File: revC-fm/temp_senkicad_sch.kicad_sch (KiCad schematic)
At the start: 4 parts, among them U24 MCP9700AT-E/LT

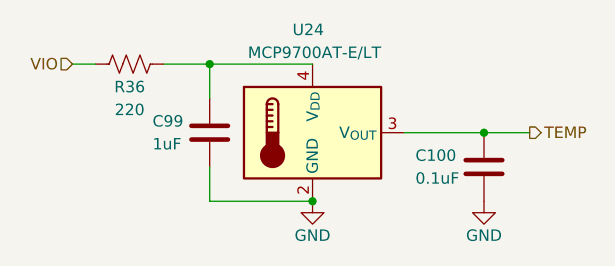
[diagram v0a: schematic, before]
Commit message: updated analog , solar comp, layout
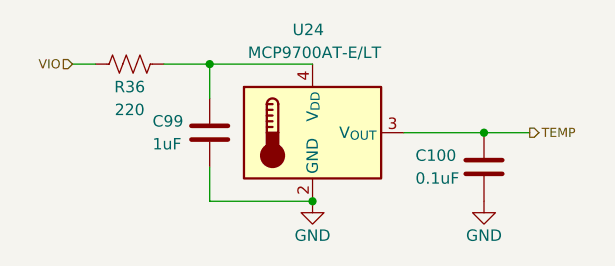
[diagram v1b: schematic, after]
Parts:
- C100: footprint Capacitor_SMD:C_0603_1608Metric -> Capacitor_SMD:C_0402_1005Metric

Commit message: routing
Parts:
- C100: footprint Capacitor_SMD:C_0402_1005Metric -> Capacitor_SMD:C_0603_1608Metric
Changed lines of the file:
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@@
         )
         (path "/d1441985-7b63-4bf8-a06d-c70da2e3b78b/cda1ad7d-3729-4e28-9f04-75ded2a9befd/8821f222-8792-4e4d-9d02-2f4e81ef493f"
-          (reference "#PWR053") (unit 1)
+          (reference "#PWR050") (unit 1)
         )
         (path "/d1441985-7b63-4bf8-a06d-c70da2e3b78b/cda1ad7d-3729-4e28-9f04-75ded2a9befd/795619f3-8bd8-4f29-a923-296e7ed8459e"
-          (reference "#PWR0148") (unit 1)
+          (reference "#PWR0158") (unit 1)
         )
         (path "/d1441985-7b63-4bf8-a06d-c70da2e3b78b/cda1ad7d-3729-4e28-9f04-75ded2a9befd/e299339d-e625-4f2c-804c-bf3cf31a6799"
-          (reference "#PWR0150") (unit 1)
+          (reference "#PWR0160") (unit 1)
         )
         (path "/d1441985-7b63-4bf8-a06d-c70da2e3b78b/cda1ad7d-3729-4e28-9f04-75ded2a9befd/ea7f9fd6-aeb6-4ec9-906e-e84511ddb647"
-          (reference "#PWR0152") (unit 1)
+          (reference "#PWR0162") (unit 1)
         )
       )
@@
         )
         (path "/d1441985-7b63-4bf8-a06d-c70da2e3b78b/cda1ad7d-3729-4e28-9f04-75ded2a9befd/795619f3-8bd8-4f29-a923-296e7ed8459e"
-          (reference "R218") (unit 1)
+          (reference "R211") (unit 1)
         )
         (path "/d1441985-7b63-4bf8-a06d-c70da2e3b78b/cda1ad7d-3729-4e28-9f04-75ded2a9befd/e299339d-e625-4f2c-804c-bf3cf31a6799"
-          (reference "R222") (unit 1)
+          (reference "R215") (unit 1)
         )
         (path "/d1441985-7b63-4bf8-a06d-c70da2e3b78b/cda1ad7d-3729-4e28-9f04-75ded2a9befd/ea7f9fd6-aeb6-4ec9-906e-e84511ddb647"
-          (reference "R223") (unit 1)
+          (reference "R216") (unit 1)
         )
       )
@@
         )
         (path "/d1441985-7b63-4bf8-a06d-c70da2e3b78b/cda1ad7d-3729-4e28-9f04-75ded2a9befd/8821f222-8792-4e4d-9d02-2f4e81ef493f"
-          (reference "U8") (unit 1)
+          (reference "U9") (unit 1)
         )
         (path "/d1441985-7b63-4bf8-a06d-c70da2e3b78b/cda1ad7d-3729-4e28-9f04-75ded2a9befd/795619f3-8bd8-4f29-a923-296e7ed8459e"
-          (reference "U26") (unit 1)
+          (reference "U29") (unit 1)
         )
         (path "/d1441985-7b63-4bf8-a06d-c70da2e3b78b/cda1ad7d-3729-4e28-9f04-75ded2a9befd/e299339d-e625-4f2c-804c-bf3cf31a6799"
-          (reference "U27") (unit 1)
+          (reference "U30") (unit 1)
         )
         (path "/d1441985-7b63-4bf8-a06d-c70da2e3b78b/cda1ad7d-3729-4e28-9f04-75ded2a9befd/ea7f9fd6-aeb6-4ec9-906e-e84511ddb647"
-          (reference "U28") (unit 1)
+          (reference "U31") (unit 1)
         )
       )
@@
         )
         (path "/d1441985-7b63-4bf8-a06d-c70da2e3b78b/cda1ad7d-3729-4e28-9f04-75ded2a9befd/8821f222-8792-4e4d-9d02-2f4e81ef493f"
-          (reference "#PWR052") (unit 1)
+          (reference "#PWR049") (unit 1)
         )
         (path "/d1441985-7b63-4bf8-a06d-c70da2e3b78b/cda1ad7d-3729-4e28-9f04-75ded2a9befd/795619f3-8bd8-4f29-a923-296e7ed8459e"
-          (reference "#PWR0147") (unit 1)
+          (reference "#PWR0157") (unit 1)
         )
         (path "/d1441985-7b63-4bf8-a06d-c70da2e3b78b/cda1ad7d-3729-4e28-9f04-75ded2a9befd/e299339d-e625-4f2c-804c-bf3cf31a6799"
-          (reference "#PWR0149") (unit 1)
+          (reference "#PWR0159") (unit 1)
         )
         (path "/d1441985-7b63-4bf8-a06d-c70da2e3b78b/cda1ad7d-3729-4e28-9f04-75ded2a9befd/ea7f9fd6-aeb6-4ec9-906e-e84511ddb647"
-          (reference "#PWR0151") (unit 1)
+          (reference "#PWR0161") (unit 1)
         )
       )
@@
       (effects (font (size 1.27 1.27)) (justify left))
     )
-    (property "Footprint" "Capacitor_SMD:C_0402_1005Metric" (at 149.5552 104.14 0)
+    (property "Footprint" "Capacitor_SMD:C_0603_1608Metric" (at 149.5552 104.14 0)
       (effects (font (size 1.27 1.27)) hide)
     )
@@
         )
         (path "/d1441985-7b63-4bf8-a06d-c70da2e3b78b/cda1ad7d-3729-4e28-9f04-75ded2a9befd/8821f222-8792-4e4d-9d02-2f4e81ef493f"
-          (reference "C35") (unit 1)
+          (reference "C36") (unit 1)
         )
         (path "/d1441985-7b63-4bf8-a06d-c70da2e3b78b/cda1ad7d-3729-4e28-9f04-75ded2a9befd/795619f3-8bd8-4f29-a923-296e7ed8459e"
-          (reference "C109") (unit 1)
+          (reference "C123") (unit 1)
         )
         (path "/d1441985-7b63-4bf8-a06d-c70da2e3b78b/cda1ad7d-3729-4e28-9f04-75ded2a9befd/e299339d-e625-4f2c-804c-bf3cf31a6799"
-          (reference "C112") (unit 1)
+          (reference "C126") (unit 1)
         )
         (path "/d1441985-7b63-4bf8-a06d-c70da2e3b78b/cda1ad7d-3729-4e28-9f04-75ded2a9befd/ea7f9fd6-aeb6-4ec9-906e-e84511ddb647"
-          (reference "C114") (unit 1)
+          (reference "C128") (unit 1)
         )
       )
@@
         )
         (path "/d1441985-7b63-4bf8-a06d-c70da2e3b78b/cda1ad7d-3729-4e28-9f04-75ded2a9befd/8821f222-8792-4e4d-9d02-2f4e81ef493f"
-          (reference "C34") (unit 1)
+          (reference "C35") (unit 1)
         )
         (path "/d1441985-7b63-4bf8-a06d-c70da2e3b78b/cda1ad7d-3729-4e28-9f04-75ded2a9befd/795619f3-8bd8-4f29-a923-296e7ed8459e"
-          (reference "C108") (unit 1)
+          (reference "C122") (unit 1)
         )
         (path "/d1441985-7b63-4bf8-a06d-c70da2e3b78b/cda1ad7d-3729-4e28-9f04-75ded2a9befd/e299339d-e625-4f2c-804c-bf3cf31a6799"
-          (reference "C111") (unit 1)
+          (reference "C125") (unit 1)
         )
         (path "/d1441985-7b63-4bf8-a06d-c70da2e3b78b/cda1ad7d-3729-4e28-9f04-75ded2a9befd/ea7f9fd6-aeb6-4ec9-906e-e84511ddb647"
-          (reference "C113") (unit 1)
+          (reference "C127") (unit 1)
         )
       )

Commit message: working revC
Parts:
- C100: footprint Capacitor_SMD:C_0603_1608Metric -> Capacitor_SMD:C_0402_1005Metric
- U24: Mfr. Part No (none) -> MCP9700AT-E/LT
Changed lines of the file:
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@@
         )
         (path "/d1441985-7b63-4bf8-a06d-c70da2e3b78b/cda1ad7d-3729-4e28-9f04-75ded2a9befd/8821f222-8792-4e4d-9d02-2f4e81ef493f"
-          (reference "#PWR055") (unit 1)
-        )
-        (path "/d1441985-7b63-4bf8-a06d-c70da2e3b78b/cda1ad7d-3729-4e28-9f04-75ded2a9befd/795619f3-8bd8-4f29-a923-296e7ed8459e"
-          (reference "#PWR0160") (unit 1)
-        )
-        (path "/d1441985-7b63-4bf8-a06d-c70da2e3b78b/cda1ad7d-3729-4e28-9f04-75ded2a9befd/e299339d-e625-4f2c-804c-bf3cf31a6799"
-          (reference "#PWR0162") (unit 1)
-        )
-        (path "/d1441985-7b63-4bf8-a06d-c70da2e3b78b/cda1ad7d-3729-4e28-9f04-75ded2a9befd/ea7f9fd6-aeb6-4ec9-906e-e84511ddb647"
-          (reference "#PWR0164") (unit 1)
+          (reference "#PWR054") (unit 1)
+        )
+        (path "/d1441985-7b63-4bf8-a06d-c70da2e3b78b/cda1ad7d-3729-4e28-9f04-75ded2a9befd/795619f3-8bd8-4f29-a923-296e7ed8459e"
+          (reference "#PWR0140") (unit 1)
+        )
+        (path "/d1441985-7b63-4bf8-a06d-c70da2e3b78b/cda1ad7d-3729-4e28-9f04-75ded2a9befd/e299339d-e625-4f2c-804c-bf3cf31a6799"
+          (reference "#PWR0142") (unit 1)
+        )
+        (path "/d1441985-7b63-4bf8-a06d-c70da2e3b78b/cda1ad7d-3729-4e28-9f04-75ded2a9befd/ea7f9fd6-aeb6-4ec9-906e-e84511ddb647"
+          (reference "#PWR0144") (unit 1)
         )
       )
@@
         )
         (path "/d1441985-7b63-4bf8-a06d-c70da2e3b78b/cda1ad7d-3729-4e28-9f04-75ded2a9befd/8821f222-8792-4e4d-9d02-2f4e81ef493f"
-          (reference "R32") (unit 1)
-        )
-        (path "/d1441985-7b63-4bf8-a06d-c70da2e3b78b/cda1ad7d-3729-4e28-9f04-75ded2a9befd/795619f3-8bd8-4f29-a923-296e7ed8459e"
-          (reference "R222") (unit 1)
-        )
-        (path "/d1441985-7b63-4bf8-a06d-c70da2e3b78b/cda1ad7d-3729-4e28-9f04-75ded2a9befd/e299339d-e625-4f2c-804c-bf3cf31a6799"
-          (reference "R228") (unit 1)
-        )
-        (path "/d1441985-7b63-4bf8-a06d-c70da2e3b78b/cda1ad7d-3729-4e28-9f04-75ded2a9befd/ea7f9fd6-aeb6-4ec9-906e-e84511ddb647"
-          (reference "R229") (unit 1)
+          (reference "R30") (unit 1)
+        )
+        (path "/d1441985-7b63-4bf8-a06d-c70da2e3b78b/cda1ad7d-3729-4e28-9f04-75ded2a9befd/795619f3-8bd8-4f29-a923-296e7ed8459e"
+          (reference "R153") (unit 1)
+        )
+        (path "/d1441985-7b63-4bf8-a06d-c70da2e3b78b/cda1ad7d-3729-4e28-9f04-75ded2a9befd/e299339d-e625-4f2c-804c-bf3cf31a6799"
+          (reference "R160") (unit 1)
+        )
+        (path "/d1441985-7b63-4bf8-a06d-c70da2e3b78b/cda1ad7d-3729-4e28-9f04-75ded2a9befd/ea7f9fd6-aeb6-4ec9-906e-e84511ddb647"
+          (reference "R161") (unit 1)
         )
       )
@@
       (effects (font (size 1.27 1.27)) hide)
     )
-    (property "Mfr. Part No" "" (at 129.54 96.52 0)
+    (property "Mfr. Part No" "MCP9700AT-E/LT" (at 129.54 96.52 0)
       (effects (font (size 1.27 1.27)) hide)
     )
@@
         )
         (path "/d1441985-7b63-4bf8-a06d-c70da2e3b78b/cda1ad7d-3729-4e28-9f04-75ded2a9befd/795619f3-8bd8-4f29-a923-296e7ed8459e"
+          (reference "U27") (unit 1)
+        )
+        (path "/d1441985-7b63-4bf8-a06d-c70da2e3b78b/cda1ad7d-3729-4e28-9f04-75ded2a9befd/e299339d-e625-4f2c-804c-bf3cf31a6799"
           (reference "U28") (unit 1)
         )
-        (path "/d1441985-7b63-4bf8-a06d-c70da2e3b78b/cda1ad7d-3729-4e28-9f04-75ded2a9befd/e299339d-e625-4f2c-804c-bf3cf31a6799"
+        (path "/d1441985-7b63-4bf8-a06d-c70da2e3b78b/cda1ad7d-3729-4e28-9f04-75ded2a9befd/ea7f9fd6-aeb6-4ec9-906e-e84511ddb647"
           (reference "U29") (unit 1)
-        )
-        (path "/d1441985-7b63-4bf8-a06d-c70da2e3b78b/cda1ad7d-3729-4e28-9f04-75ded2a9befd/ea7f9fd6-aeb6-4ec9-906e-e84511ddb647"
-          (reference "U30") (unit 1)
         )
       )
@@
         )
         (path "/d1441985-7b63-4bf8-a06d-c70da2e3b78b/cda1ad7d-3729-4e28-9f04-75ded2a9befd/8821f222-8792-4e4d-9d02-2f4e81ef493f"
-          (reference "#PWR054") (unit 1)
-        )
-        (path "/d1441985-7b63-4bf8-a06d-c70da2e3b78b/cda1ad7d-3729-4e28-9f04-75ded2a9befd/795619f3-8bd8-4f29-a923-296e7ed8459e"
-          (reference "#PWR0159") (unit 1)
-        )
-        (path "/d1441985-7b63-4bf8-a06d-c70da2e3b78b/cda1ad7d-3729-4e28-9f04-75ded2a9befd/e299339d-e625-4f2c-804c-bf3cf31a6799"
-          (reference "#PWR0161") (unit 1)
-        )
-        (path "/d1441985-7b63-4bf8-a06d-c70da2e3b78b/cda1ad7d-3729-4e28-9f04-75ded2a9befd/ea7f9fd6-aeb6-4ec9-906e-e84511ddb647"
-          (reference "#PWR0163") (unit 1)
+          (reference "#PWR053") (unit 1)
+        )
+        (path "/d1441985-7b63-4bf8-a06d-c70da2e3b78b/cda1ad7d-3729-4e28-9f04-75ded2a9befd/795619f3-8bd8-4f29-a923-296e7ed8459e"
+          (reference "#PWR0139") (unit 1)
+        )
+        (path "/d1441985-7b63-4bf8-a06d-c70da2e3b78b/cda1ad7d-3729-4e28-9f04-75ded2a9befd/e299339d-e625-4f2c-804c-bf3cf31a6799"
+          (reference "#PWR0141") (unit 1)
+        )
+        (path "/d1441985-7b63-4bf8-a06d-c70da2e3b78b/cda1ad7d-3729-4e28-9f04-75ded2a9befd/ea7f9fd6-aeb6-4ec9-906e-e84511ddb647"
+          (reference "#PWR0143") (unit 1)
         )
       )
@@
       (effects (font (size 1.27 1.27)) (justify left))
     )
-    (property "Footprint" "Capacitor_SMD:C_0603_1608Metric" (at 149.5552 104.14 0)
+    (property "Footprint" "Capacitor_SMD:C_0402_1005Metric" (at 149.5552 104.14 0)
       (effects (font (size 1.27 1.27)) hide)
     )
@@
         )
         (path "/d1441985-7b63-4bf8-a06d-c70da2e3b78b/cda1ad7d-3729-4e28-9f04-75ded2a9befd/8821f222-8792-4e4d-9d02-2f4e81ef493f"
-          (reference "C37") (unit 1)
-        )
-        (path "/d1441985-7b63-4bf8-a06d-c70da2e3b78b/cda1ad7d-3729-4e28-9f04-75ded2a9befd/795619f3-8bd8-4f29-a923-296e7ed8459e"
-          (reference "C114") (unit 1)
-        )
-        (path "/d1441985-7b63-4bf8-a06d-c70da2e3b78b/cda1ad7d-3729-4e28-9f04-75ded2a9befd/e299339d-e625-4f2c-804c-bf3cf31a6799"
-          (reference "C117") (unit 1)
-        )
-        (path "/d1441985-7b63-4bf8-a06d-c70da2e3b78b/cda1ad7d-3729-4e28-9f04-75ded2a9befd/ea7f9fd6-aeb6-4ec9-906e-e84511ddb647"
-          (reference "C119") (unit 1)
+          (reference "C36") (unit 1)
+        )
+        (path "/d1441985-7b63-4bf8-a06d-c70da2e3b78b/cda1ad7d-3729-4e28-9f04-75ded2a9befd/795619f3-8bd8-4f29-a923-296e7ed8459e"
+          (reference "C98") (unit 1)
+        )
+        (path "/d1441985-7b63-4bf8-a06d-c70da2e3b78b/cda1ad7d-3729-4e28-9f04-75ded2a9befd/e299339d-e625-4f2c-804c-bf3cf31a6799"
+          (reference "C101") (unit 1)
+        )
+        (path "/d1441985-7b63-4bf8-a06d-c70da2e3b78b/cda1ad7d-3729-4e28-9f04-75ded2a9befd/ea7f9fd6-aeb6-4ec9-906e-e84511ddb647"
+          (reference "C103") (unit 1)
         )
       )
@@
         )
         (path "/d1441985-7b63-4bf8-a06d-c70da2e3b78b/cda1ad7d-3729-4e28-9f04-75ded2a9befd/8821f222-8792-4e4d-9d02-2f4e81ef493f"
-          (reference "C36") (unit 1)
-        )
-        (path "/d1441985-7b63-4bf8-a06d-c70da2e3b78b/cda1ad7d-3729-4e28-9f04-75ded2a9befd/795619f3-8bd8-4f29-a923-296e7ed8459e"
-          (reference "C113") (unit 1)
-        )
-        (path "/d1441985-7b63-4bf8-a06d-c70da2e3b78b/cda1ad7d-3729-4e28-9f04-75ded2a9befd/e299339d-e625-4f2c-804c-bf3cf31a6799"
-          (reference "C116") (unit 1)
-        )
-        (path "/d1441985-7b63-4bf8-a06d-c70da2e3b78b/cda1ad7d-3729-4e28-9f04-75ded2a9befd/ea7f9fd6-aeb6-4ec9-906e-e84511ddb647"
-          (reference "C118") (unit 1)
-        )
-      )
+          (reference "C35") (unit 1)
+        )
+        (path "/d1441985-7b63-4bf8-a06d-c70da2e3b78b/cda1ad7d-3729-4e28-9f04-75ded2a9befd/795619f3-8bd8-4f29-a923-296e7ed8459e"
+          (reference "C97") (unit 1)
+        )
+        (path "/d1441985-7b63-4bf8-a06d-c70da2e3b78b/cda1ad7d-3729-4e28-9f04-75ded2a9befd/e299339d-e625-4f2c-804c-bf3cf31a6799"
+          (reference "C100") (unit 1)
+        )
+        (path "/d1441985-7b63-4bf8-a06d-c70da2e3b78b/cda1ad7d-3729-4e28-9f04-75ded2a9befd/ea7f9fd6-aeb6-4ec9-906e-e84511ddb647"
+          (reference "C102") (unit 1)
+        )
+      )

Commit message: almost done!!!!!
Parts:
- renumbered C99 to C30, C100 to C31, R36 to R29, U24 to U9
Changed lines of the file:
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@@
   (symbol (lib_id "power:GND") (at 148.59 104.14 0) (unit 1)
     (in_bom yes) (on_board yes) (dnp no)
-    (property "Reference" "#PWR04" (at 148.59 110.49 0)
+    (property "Reference" "#PWR050" (at 148.59 110.49 0)
       (effects (font (size 1.27 1.27)) hide)
     )
@@
     (instances
       (project "mainboard"
-        (path "/d1441985-7b63-4bf8-a06d-c70da2e3b78b/00000000-0000-0000-0000-00005cec5dde/a78437db-a0fc-4cde-8346-4d17e2576807"
-          (reference "#PWR04") (unit 1)
-        )
         (path "/d1441985-7b63-4bf8-a06d-c70da2e3b78b/cda1ad7d-3729-4e28-9f04-75ded2a9befd/8821f222-8792-4e4d-9d02-2f4e81ef493f"
           (reference "#PWR050") (unit 1)
@@
   (symbol (lib_id "Device:R_US") (at 109.22 88.9 90) (unit 1)
     (in_bom yes) (on_board yes) (dnp no)
-    (property "Reference" "R36" (at 109.22 91.44 90)
+    (property "Reference" "R29" (at 109.22 91.44 90)
       (effects (font (size 1.27 1.27)))
     )
@@
     (instances
       (project "mainboard"
-        (path "/d1441985-7b63-4bf8-a06d-c70da2e3b78b/00000000-0000-0000-0000-00005cec5dde/a78437db-a0fc-4cde-8346-4d17e2576807"
-          (reference "R36") (unit 1)
-        )
         (path "/d1441985-7b63-4bf8-a06d-c70da2e3b78b/cda1ad7d-3729-4e28-9f04-75ded2a9befd/8821f222-8792-4e4d-9d02-2f4e81ef493f"
           (reference "R29") (unit 1)
@@
   (symbol (lib_id "Sensor_Temperature:MCP9700Ax-ELT") (at 129.54 96.52 0) (unit 1)
     (in_bom yes) (on_board yes) (dnp no)
-    (property "Reference" "U24" (at 130.81 85.09 0)
+    (property "Reference" "U9" (at 130.81 85.09 0)
       (effects (font (size 1.27 1.27)) (justify right))
     )
@@
     (instances
       (project "mainboard"
-        (path "/d1441985-7b63-4bf8-a06d-c70da2e3b78b/00000000-0000-0000-0000-00005cec5dde/a78437db-a0fc-4cde-8346-4d17e2576807"
-          (reference "U24") (unit 1)
-        )
         (path "/d1441985-7b63-4bf8-a06d-c70da2e3b78b/cda1ad7d-3729-4e28-9f04-75ded2a9befd/8821f222-8792-4e4d-9d02-2f4e81ef493f"
           (reference "U9") (unit 1)
@@
   (symbol (lib_id "power:GND") (at 129.54 104.14 0) (unit 1)
     (in_bom yes) (on_board yes) (dnp no)
-    (property "Reference" "#PWR0136" (at 129.54 110.49 0)
+    (property "Reference" "#PWR049" (at 129.54 110.49 0)
       (effects (font (size 1.27 1.27)) hide)
     )
@@
     (instances
       (project "mainboard"
-        (path "/d1441985-7b63-4bf8-a06d-c70da2e3b78b/00000000-0000-0000-0000-00005cec5dde/a78437db-a0fc-4cde-8346-4d17e2576807"
-          (reference "#PWR0136") (unit 1)
-        )
         (path "/d1441985-7b63-4bf8-a06d-c70da2e3b78b/cda1ad7d-3729-4e28-9f04-75ded2a9befd/8821f222-8792-4e4d-9d02-2f4e81ef493f"
           (reference "#PWR049") (unit 1)
@@
   (symbol (lib_id "Device:C") (at 148.59 100.33 0) (unit 1)
     (in_bom yes) (on_board yes) (dnp no)
-    (property "Reference" "C100" (at 140.97 99.06 0)
+    (property "Reference" "C31" (at 140.97 99.06 0)
       (effects (font (size 1.27 1.27)) (justify left))
     )
@@
     (instances
       (project "mainboard"
-        (path "/d1441985-7b63-4bf8-a06d-c70da2e3b78b/00000000-0000-0000-0000-00005cec5dde/a78437db-a0fc-4cde-8346-4d17e2576807"
-          (reference "C100") (unit 1)
-        )
         (path "/d1441985-7b63-4bf8-a06d-c70da2e3b78b/cda1ad7d-3729-4e28-9f04-75ded2a9befd/8821f222-8792-4e4d-9d02-2f4e81ef493f"
           (reference "C31") (unit 1)
@@
   (symbol (lib_id "Device:C") (at 118.11 96.52 0) (unit 1)
     (in_bom yes) (on_board yes) (dnp no)
-    (property "Reference" "C99" (at 111.76 95.25 0)
+    (property "Reference" "C30" (at 111.76 95.25 0)
       (effects (font (size 1.27 1.27)) (justify left))
     )
@@
     (instances
       (project "mainboard"
-        (path "/d1441985-7b63-4bf8-a06d-c70da2e3b78b/00000000-0000-0000-0000-00005cec5dde/a78437db-a0fc-4cde-8346-4d17e2576807"
-          (reference "C99") (unit 1)
-        )
         (path "/d1441985-7b63-4bf8-a06d-c70da2e3b78b/cda1ad7d-3729-4e28-9f04-75ded2a9befd/8821f222-8792-4e4d-9d02-2f4e81ef493f"
           (reference "C30") (unit 1)

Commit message: updated fab files
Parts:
- C112: renamed from C30; Manufacturer (none) -> TDK; Mfr. Part No (none) -> CGA3E1X7R1V105K080AE
- C113: renamed from C31; Manufacturer (none) -> TDK; Mfr. Part No (none) -> CGA2B3X7R1H104K050BE
- R251: renamed from R29; Manufacturer (none) -> Stackpole Electronics; Mfr. Part No (none) -> RMCF0603FT220R
- U32: renamed from U9; Manufacturer (none) -> Microchip Technology
